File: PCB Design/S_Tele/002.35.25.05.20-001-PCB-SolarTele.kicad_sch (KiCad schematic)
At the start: 33 parts, among them J1 Screw_Terminal_01x08, J2 Conn_01x01, J3 SMA, J4 SMA, J5 SMA, J6 SMA, J7 SMA, J8 SMA, U1 L7815, U2 L7805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

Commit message: Fixed footprint assignments in schematic
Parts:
- R1, R12, R15, R2, R6, R9: footprint Resistor_SMD:R_1206_3216Metric -> Resistor_SMD:R_0805_2012Metric

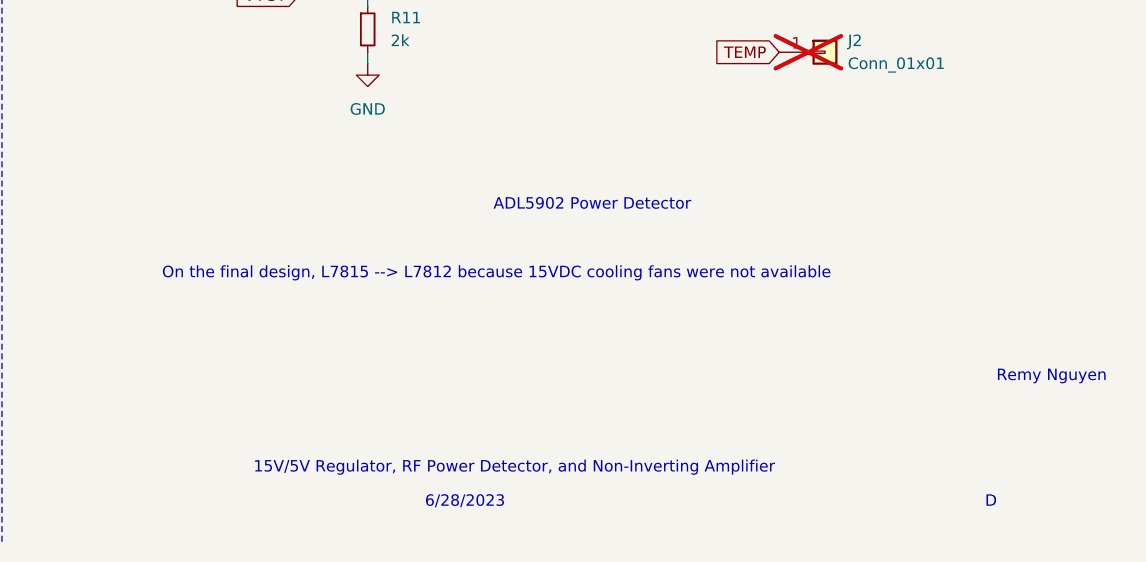
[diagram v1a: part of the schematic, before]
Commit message: Sch. comment: op-amp topology is incorrect
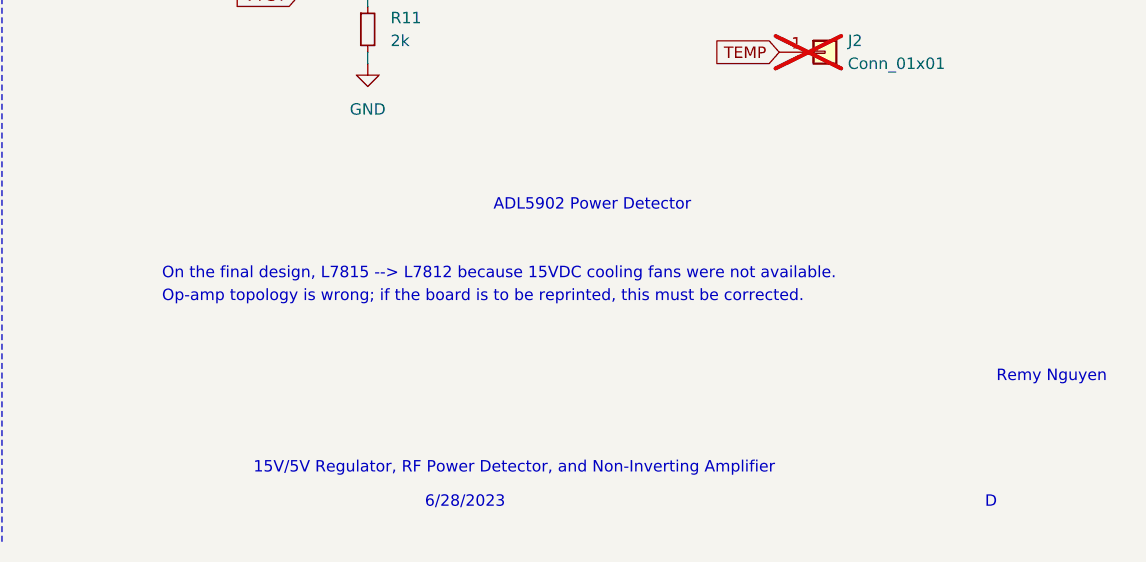
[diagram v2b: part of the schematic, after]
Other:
- note added: "On the final design, L7815 --> L7812 because 15VDC cooling fans were not available."
- note added: "Op-amp topology is wrong; if the board is to be reprinted, this must be corrected."
- note removed: "On the final design, L7815 --> L7812 because 15VDC cooling fans were not available"
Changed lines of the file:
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@@
+    (effects (font (size 1.27 1.27)) (justify left bottom))
+  )
+  (text "Op-amp topology is wrong; if the board is to be reprinted, this must be corrected."
+    (at 177.8 171.45 0)
     (effects (font (size 1.27 1.27)) (justify left bottom))
   )
@@
     (effects (font (size 1.27 1.27)) (justify left bottom))
   )
-  (text "On the final design, L7815 --> L7812 because 15VDC cooling fans were not available"
+  (text "On the final design, L7815 --> L7812 because 15VDC cooling fans were not available."
     (at 177.8 168.91 0)
     (effects (font (size 1.27 1.27)) (justify left bottom))
